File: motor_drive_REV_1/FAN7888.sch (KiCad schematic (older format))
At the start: 7 parts

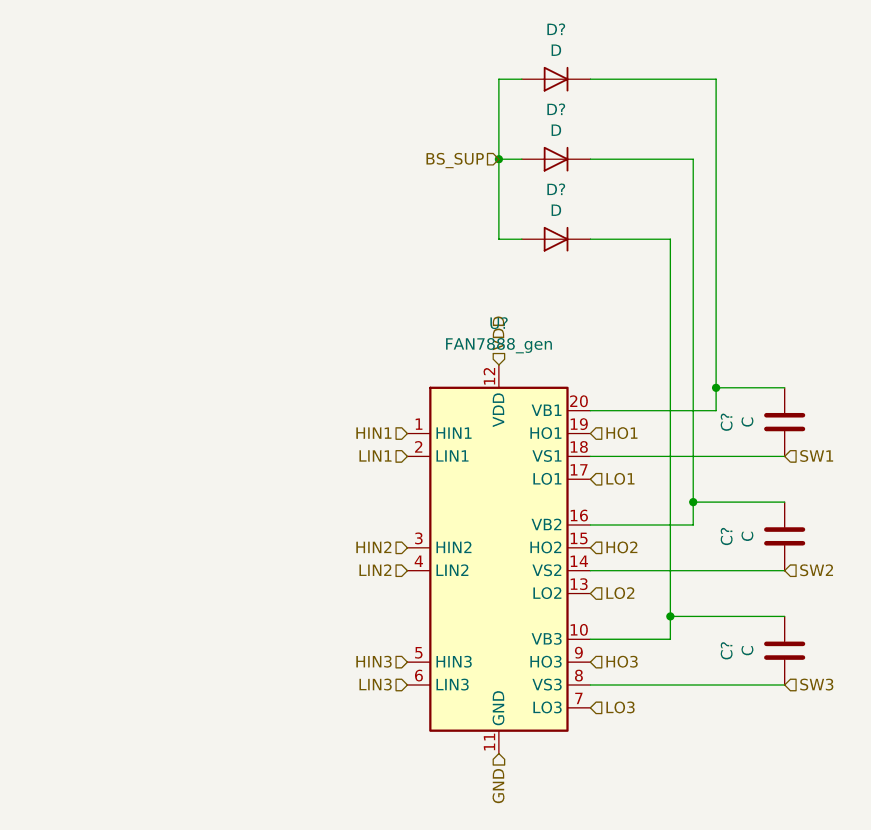
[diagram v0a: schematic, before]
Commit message: organizing pinout and BOM
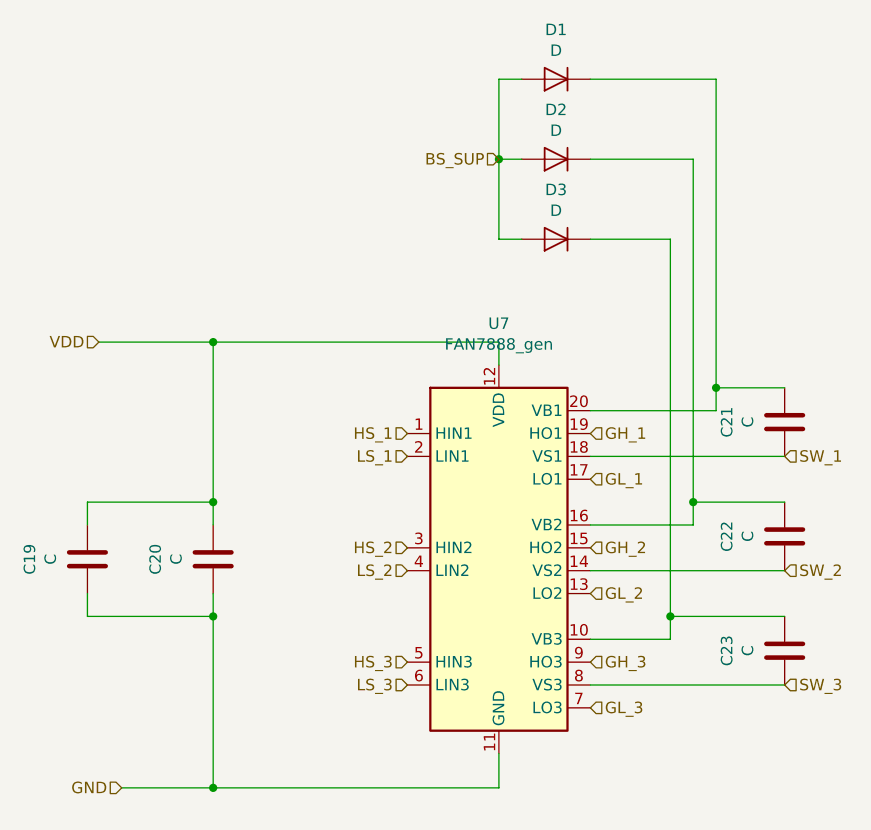
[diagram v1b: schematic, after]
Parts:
- added C19, C20: C, motor_drive_footprints:C_0603_1608Metric, symbol motor_drive:C
- C21, C22, C23: renamed from C?; footprint (none) -> motor_drive_footprints:C_0603_1608Metric
- D1, D2, D3: renamed from D?; footprint (none) -> motor_drive_footprints:SOD123
- U7: renamed from U?; footprint Package_SO:SOIC-20W_7.5x12.8mm_P1.27mm -> motor_drive_footprints:FAN7888
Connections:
- net GND: now also C19.2, C20.2
- net VDD: now also C19.1, C20.1
- net HIN1 renamed HS_1
- net HIN2 renamed HS_2
- net HIN3 renamed HS_3
- net HO1 renamed GH_1
- net HO2 renamed GH_2
- net HO3 renamed GH_3
- net LIN1 renamed LS_1
- net LIN2 renamed LS_2
- net LIN3 renamed LS_3
- net LO1 renamed GL_1
- net LO2 renamed GL_2
- net LO3 renamed GL_3
- net SW1 renamed SW_1
- net SW2 renamed SW_2
- net SW3 renamed SW_3
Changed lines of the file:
@@
 $Descr A4 11693 8268
 encoding utf-8
-Sheet 7 14
+Sheet 12 14
 Title ""
 Date ""
@@
 $EndDescr
 $Comp
-L motor_drive:FAN7888_gen U?
+L motor_drive:FAN7888_gen U7
 U 1 1 5E28F58F
 P 5350 3450
-F 0 "U?" H 5350 4531 50  0000 C CNN
+F 0 "U7" H 5350 4531 50  0000 C CNN
 F 1 "FAN7888_gen" H 5350 4440 50  0000 C CNN
-F 2 "Package_SO:SOIC-20W_7.5x12.8mm_P1.27mm" H 5400 2700 50  0001 L CNN
+F 2 "motor_drive_footprints:FAN7888" H 5400 2700 50  0001 L CNN
 F 3 "http://www.onsemi.com/pub/Collateral/FAN7888-D.pdf" H 5350 3450 50  0001 C CNN
 	1    5350 3450
@@
 $EndComp
 $Comp
-L motor_drive:C C?
+L motor_drive:C C21
 U 1 1 5E290119
 P 6600 2800
-F 0 "C?" V 6348 2800 50  0000 C CNN
+F 0 "C21" V 6348 2800 50  0000 C CNN
 F 1 "C" V 6439 2800 50  0000 C CNN
-F 2 "" H 6638 2650 50  0001 C CNN
+F 2 "motor_drive_footprints:C_0603_1608Metric" H 6638 2650 50  0001 C CNN
 F 3 "~" H 6600 2800 50  0001 C CNN
 	1    6600 2800
@@
 $EndComp
 Text HLabel 5750 2850 2    50   Input ~ 0
-HO1
+GH_1
 Text HLabel 5750 3050 2    50   Input ~ 0
-LO1
-$Comp
-L motor_drive:C C?
+GL_1
+$Comp
+L motor_drive:C C22
 U 1 1 5E291813
 P 6600 3300
-F 0 "C?" V 6348 3300 50  0000 C CNN
+F 0 "C22" V 6348 3300 50  0000 C CNN
 F 1 "C" V 6439 3300 50  0000 C CNN
-F 2 "" H 6638 3150 50  0001 C CNN
+F 2 "motor_drive_footprints:C_0603_1608Metric" H 6638 3150 50  0001 C CNN
 F 3 "~" H 6600 3300 50  0001 C CNN
 	1    6600 3300
@@
 $EndComp
 $Comp
-L motor_drive:C C?
+L motor_drive:C C23
 U 1 1 5E291C33
 P 6600 3800
-F 0 "C?" V 6348 3800 50  0000 C CNN
+F 0 "C23" V 6348 3800 50  0000 C CNN
 F 1 "C" V 6439 3800 50  0000 C CNN
-F 2 "" H 6638 3650 50  0001 C CNN
+F 2 "motor_drive_footprints:C_0603_1608Metric" H 6638 3650 50  0001 C CNN
 F 3 "~" H 6600 3800 50  0001 C CNN
 	1    6600 3800
@@
 	5750 3750 6100 3750
 Text HLabel 5750 3350 2    50   Input ~ 0
-HO2
+GH_2
 Text HLabel 5750 3550 2    50   Input ~ 0
-LO2
+GL_2
 Text HLabel 5750 3850 2    50   Input ~ 0
-HO3
+GH_3
 Text HLabel 5750 4050 2    50   Input ~ 0
-LO3
+GL_3
 Text HLabel 6600 2950 2    50   Input ~ 0
-SW1
+SW_1
 Text HLabel 6600 3450 2    50   Input ~ 0
-SW2
+SW_2
 Text HLabel 6600 3950 2    50   Input ~ 0
-SW3
-$Comp
-L motor_drive:D D?
+SW_3
+$Comp
+L motor_drive:D D1
 U 1 1 5E2967E8
 P 5600 1300
-F 0 "D?" H 5600 1084 50  0000 C CNN
+F 0 "D1" H 5600 1084 50  0000 C CNN
 F 1 "D" H 5600 1175 50  0000 C CNN
-F 2 "" H 5600 1300 50  0001 C CNN
+F 2 "motor_drive_footprints:SOD123" H 5600 1300 50  0001 C CNN
 F 3 "~" H 5600 1300 50  0001 C CNN
 	1    5600 1300
@@
 $EndComp
 $Comp
-L motor_drive:D D?
+L motor_drive:D D2
 U 1 1 5E296FA9
 P 5600 1650
-F 0 "D?" H 5600 1434 50  0000 C CNN
+F 0 "D2" H 5600 1434 50  0000 C CNN
 F 1 "D" H 5600 1525 50  0000 C CNN
-F 2 "" H 5600 1650 50  0001 C CNN
+F 2 "motor_drive_footprints:SOD123" H 5600 1650 50  0001 C CNN
 F 3 "~" H 5600 1650 50  0001 C CNN
 	1    5600 1650
@@
 $EndComp
 $Comp
-L motor_drive:D D?
+L motor_drive:D D3
 U 1 1 5E2971E1
 P 5600 2000
-F 0 "D?" H 5600 1784 50  0000 C CNN
+F 0 "D3" H 5600 1784 50  0000 C CNN
 F 1 "D" H 5600 1875 50  0000 C CNN
-F 2 "" H 5600 2000 50  0001 C CNN
+F 2 "motor_drive_footprints:SOD123" H 5600 2000 50  0001 C CNN
 F 3 "~" H 5600 2000 50  0001 C CNN
 	1    5600 2000
@@
 Connection ~ 6100 3650
 Text HLabel 4950 2850 0    50   Input ~ 0
-HIN1
+HS_1
 Text HLabel 4950 2950 0    50   Input ~ 0
-LIN1
+LS_1
 Text HLabel 4950 3350 0    50   Input ~ 0
-HIN2
+HS_2
 Text HLabel 4950 3450 0    50   Input ~ 0
-LIN2
+LS_2
 Text HLabel 4950 3850 0    50   Input ~ 0
-HIN3
+HS_3
 Text HLabel 4950 3950 0    50   Input ~ 0
-LIN3
-Text HLabel 5350 4250 3    50   Input ~ 0
+LS_3
+Text HLabel 3700 4400 0    50   Input ~ 0
 GND
-Text HLabel 5350 2550 1    50   Input ~ 0
+Text HLabel 3600 2450 0    50   Input ~ 0
 VDD
 Wire Wire Line
@@
 Text HLabel 5350 1650 0    50   Input ~ 0
 BS_SUP
+Wire Wire Line
+	5350 2550 5350 2450
+Wire Wire Line
+	5350 4250 5350 4400
+Wire Wire Line
+	4100 4400 3700 4400
+Wire Wire Line
+	5350 4400 4100 4400
+Connection ~ 4100 4400
+Wire Wire Line
+	4100 3650 4100 4400
+Wire Wire Line
+	3550 3650 4100 3650
+Wire Wire Line
+	3550 3550 3550 3650
+Wire Wire Line
+	4100 2450 3600 2450
+Wire Wire Line
+	5350 2450 4100 2450
+Connection ~ 4100 2450
+Wire Wire Line
+	4100 3150 4100 2450
+Wire Wire Line
+	3550 3150 4100 3150
+Wire Wire Line
+	3550 3250 3550 3150
+$Comp
+L motor_drive:C C19
+U 1 1 5E3AA0F7
+P 3550 3400
+F 0 "C19" V 3298 3400 50  0000 C CNN
+F 1 "C" V 3389 3400 50  0000 C CNN
+F 2 "motor_drive_footprints:C_0603_1608Metric" H 3588 3250 50  0001 C CNN
+F 3 "~" H 3550 3400 50  0001 C CNN
+	1    3550 3400
+	1    0    0    -1
+$EndComp
+Connection ~ 4100 3650
+Wire Wire Line
+	4100 3550 4100 3650
+Connection ~ 4100 3150
+Wire Wire Line
+	4100 3250 4100 3150
+$Comp
+L motor_drive:C C20
+U 1 1 5E3A6EC9
+P 4100 3400
+F 0 "C20" V 3848 3400 50  0000 C CNN
+F 1 "C" V 3939 3400 50  0000 C CNN
+F 2 "motor_drive_footprints:C_0603_1608Metric" H 4138 3250 50  0001 C CNN
+F 3 "~" H 4100 3400 50  0001 C CNN
+	1    4100 3400
+	1    0    0    -1
+$EndComp
 $EndSCHEMATC

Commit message: working on adding thermistors but encountered too many hierarchicaly copies bug
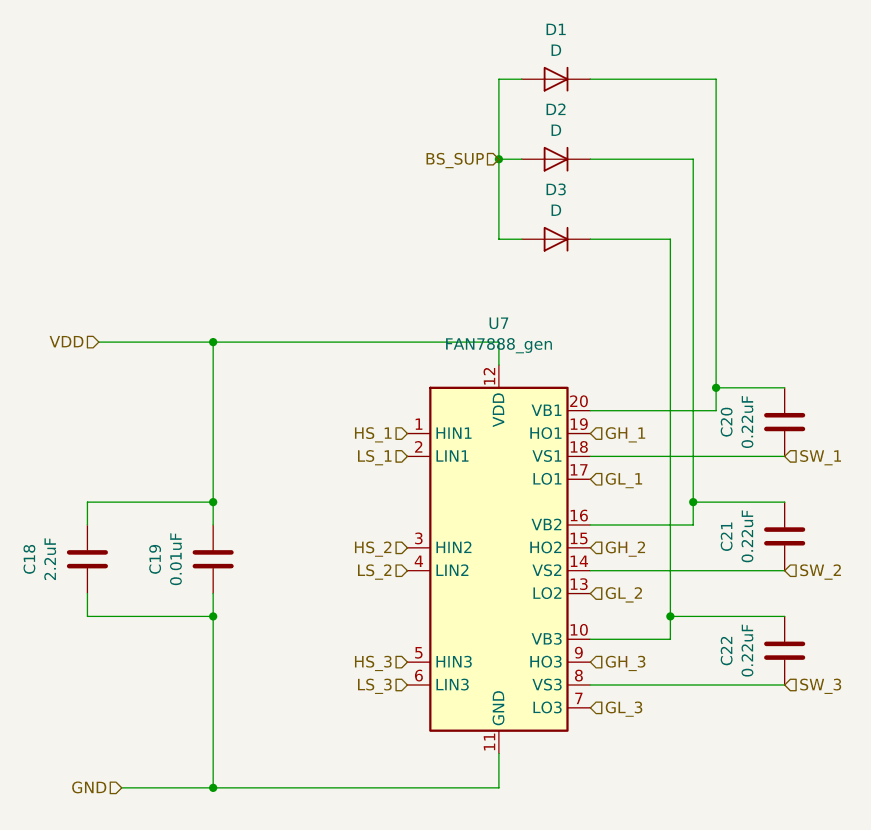
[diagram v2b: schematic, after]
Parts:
- C18: renamed from C19; value C -> 2.2uF
- C19: renamed from C20; value C -> 0.01uF
- C20: renamed from C21; value C -> 0.22uF
- C21: renamed from C22; value C -> 0.22uF
- C22: renamed from C23; value C -> 0.22uF
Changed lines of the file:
@@
 $EndComp
 $Comp
-L motor_drive:C C21
+L motor_drive:C C20
 U 1 1 5E290119
 P 6600 2800
-F 0 "C21" V 6348 2800 50  0000 C CNN
-F 1 "C" V 6439 2800 50  0000 C CNN
+F 0 "C20" V 6348 2800 50  0000 C CNN
+F 1 "0.22uF" V 6439 2800 50  0000 C CNN
 F 2 "motor_drive_footprints:C_0603_1608Metric" H 6638 2650 50  0001 C CNN
 F 3 "~" H 6600 2800 50  0001 C CNN
@@
 GL_1
 $Comp
-L motor_drive:C C22
+L motor_drive:C C21
 U 1 1 5E291813
 P 6600 3300
-F 0 "C22" V 6348 3300 50  0000 C CNN
-F 1 "C" V 6439 3300 50  0000 C CNN
+F 0 "C21" V 6348 3300 50  0000 C CNN
+F 1 "0.22uF" V 6439 3300 50  0000 C CNN
 F 2 "motor_drive_footprints:C_0603_1608Metric" H 6638 3150 50  0001 C CNN
 F 3 "~" H 6600 3300 50  0001 C CNN
@@
 $EndComp
 $Comp
-L motor_drive:C C23
+L motor_drive:C C22
 U 1 1 5E291C33
 P 6600 3800
-F 0 "C23" V 6348 3800 50  0000 C CNN
-F 1 "C" V 6439 3800 50  0000 C CNN
+F 0 "C22" V 6348 3800 50  0000 C CNN
+F 1 "0.22uF" V 6439 3800 50  0000 C CNN
 F 2 "motor_drive_footprints:C_0603_1608Metric" H 6638 3650 50  0001 C CNN
 F 3 "~" H 6600 3800 50  0001 C CNN
@@
 	3550 3250 3550 3150
 $Comp
-L motor_drive:C C19
+L motor_drive:C C18
 U 1 1 5E3AA0F7
 P 3550 3400
-F 0 "C19" V 3298 3400 50  0000 C CNN
-F 1 "C" V 3389 3400 50  0000 C CNN
+F 0 "C18" V 3298 3400 50  0000 C CNN
+F 1 "2.2uF" V 3389 3400 50  0000 C CNN
 F 2 "motor_drive_footprints:C_0603_1608Metric" H 3588 3250 50  0001 C CNN
 F 3 "~" H 3550 3400 50  0001 C CNN
@@
 	4100 3250 4100 3150
 $Comp
-L motor_drive:C C20
+L motor_drive:C C19
 U 1 1 5E3A6EC9
 P 4100 3400
-F 0 "C20" V 3848 3400 50  0000 C CNN
-F 1 "C" V 3939 3400 50  0000 C CNN
+F 0 "C19" V 3848 3400 50  0000 C CNN
+F 1 "0.01uF" V 3939 3400 50  0000 C CNN
 F 2 "motor_drive_footprints:C_0603_1608Metric" H 4138 3250 50  0001 C CNN
 F 3 "~" H 4100 3400 50  0001 C CNN

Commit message: started layout
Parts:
- renumbered C18 to C27, C19 to C28, C20 to C29, C21 to C30, C22 to C31
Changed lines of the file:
@@
 $Descr A4 11693 8268
 encoding utf-8
-Sheet 12 14
+Sheet 12 16
 Title ""
 Date ""
@@
 $EndComp
 $Comp
-L motor_drive:C C20
+L motor_drive:C C29
 U 1 1 5E290119
 P 6600 2800
-F 0 "C20" V 6348 2800 50  0000 C CNN
+F 0 "C29" V 6348 2800 50  0000 C CNN
 F 1 "0.22uF" V 6439 2800 50  0000 C CNN
 F 2 "motor_drive_footprints:C_0603_1608Metric" H 6638 2650 50  0001 C CNN
@@
 GL_1
 $Comp
-L motor_drive:C C21
+L motor_drive:C C30
 U 1 1 5E291813
 P 6600 3300
-F 0 "C21" V 6348 3300 50  0000 C CNN
+F 0 "C30" V 6348 3300 50  0000 C CNN
 F 1 "0.22uF" V 6439 3300 50  0000 C CNN
 F 2 "motor_drive_footprints:C_0603_1608Metric" H 6638 3150 50  0001 C CNN
@@
 $EndComp
 $Comp
-L motor_drive:C C22
+L motor_drive:C C31
 U 1 1 5E291C33
 P 6600 3800
-F 0 "C22" V 6348 3800 50  0000 C CNN
+F 0 "C31" V 6348 3800 50  0000 C CNN
 F 1 "0.22uF" V 6439 3800 50  0000 C CNN
 F 2 "motor_drive_footprints:C_0603_1608Metric" H 6638 3650 50  0001 C CNN
@@
 	3550 3250 3550 3150
 $Comp
-L motor_drive:C C18
+L motor_drive:C C27
 U 1 1 5E3AA0F7
 P 3550 3400
-F 0 "C18" V 3298 3400 50  0000 C CNN
+F 0 "C27" V 3298 3400 50  0000 C CNN
 F 1 "2.2uF" V 3389 3400 50  0000 C CNN
 F 2 "motor_drive_footprints:C_0603_1608Metric" H 3588 3250 50  0001 C CNN
@@
 	4100 3250 4100 3150
 $Comp
-L motor_drive:C C19
+L motor_drive:C C28
 U 1 1 5E3A6EC9
 P 4100 3400
-F 0 "C19" V 3848 3400 50  0000 C CNN
+F 0 "C28" V 3848 3400 50  0000 C CNN
 F 1 "0.01uF" V 3939 3400 50  0000 C CNN
 F 2 "motor_drive_footprints:C_0603_1608Metric" H 4138 3250 50  0001 C CNN
